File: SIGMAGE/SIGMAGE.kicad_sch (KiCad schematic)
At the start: 0 parts

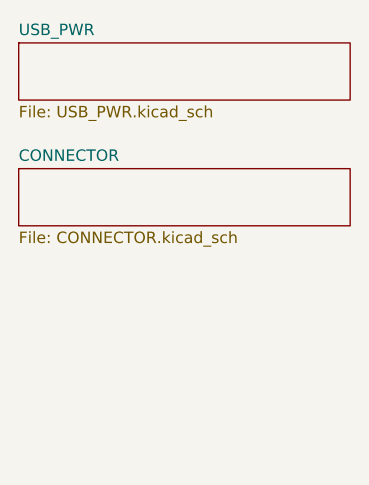
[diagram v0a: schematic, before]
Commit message: Added RJ45/PHY and MCU
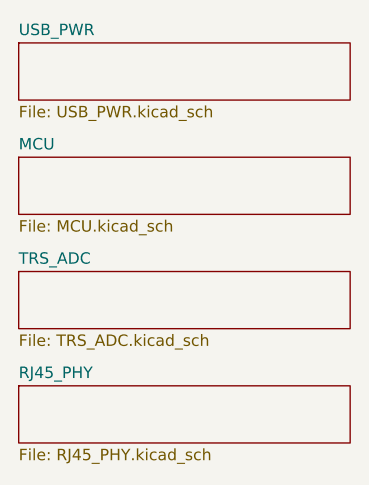
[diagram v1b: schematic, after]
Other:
- removed sheet CONNECTOR
- added sheet MCU (MCU.kicad_sch)
- added sheet RJ45_PHY (RJ45_PHY.kicad_sch)
- added sheet TRS_ADC (TRS_ADC.kicad_sch)
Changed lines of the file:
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@@
 	(paper "A4")
+	(sheet
+		(at 17.78 31.75)
+		(size 36.83 6.35)
+		(exclude_from_sim no)
+		(in_bom yes)
+		(on_board yes)
+		(dnp no)
+		(fields_autoplaced yes)
+		(stroke
+			(width 0.1524)
+			(type solid)
+		)
+		(fill
+			(color 0 0 0 0.0000)
+		)
+		(property "Sheetname" "MCU"
+			(at 17.78 31.0384 0)
+			(effects
+				(font
+					(size 1.27 1.27)
+				)
+				(justify left bottom)
+			)
+		)
+		(property "Sheetfile" "MCU.kicad_sch"
+			(at 17.78 38.6846 0)
+			(effects
+				(font
+					(size 1.27 1.27)
+				)
+				(justify left top)
+			)
+		)
+		(instances
+			(project "SIGMAGE"
+				(path "/6fbe3371-b6a3-4e28-aef4-4e5865f4674e"
+					(page "4")
+				)
+			)
+		)
+	)
 	(sheet
 		(at 17.78 19.05)
@@
 	)
 	(sheet
-		(at 17.78 33.02)
+		(at 17.78 44.45)
 		(size 36.83 6.35)
 		(exclude_from_sim no)
@@
 			(color 0 0 0 0.0000)
 		)
-		(property "Sheetname" "CONNECTOR"
-			(at 17.78 32.3084 0)
+		(property "Sheetname" "TRS_ADC"
+			(at 17.78 43.7384 0)
 			(effects
 				(font
@@
 			)
 		)
-		(property "Sheetfile" "CONNECTOR.kicad_sch"
-			(at 17.78 39.9546 0)
+		(property "Sheetfile" "TRS_ADC.kicad_sch"
+			(at 17.78 51.3846 0)
 			(effects
 				(font
@@
 			(project "SIGMAGE"
 				(path "/6fbe3371-b6a3-4e28-aef4-4e5865f4674e"
-					(page "3")
+					(page "5")
 				)
 			)
+		)
+	)
+	(sheet
+		(at 17.78 57.15)
+		(size 36.83 6.35)
+		(exclude_from_sim no)
+		(in_bom yes)
+		(on_board yes)
+		(dnp no)
+		(fields_autoplaced yes)
+		(stroke
+			(width 0.1524)
+			(type solid)
+		)
+		(fill
+			(color 0 0 0 0.0000)
+		)
+		(property "Sheetname" "RJ45_PHY"
+			(at 17.78 56.4384 0)
+			(effects
+				(font
+					(size 1.27 1.27)
+				)
+				(justify left bottom)
+			)
+		)
+		(property "Sheetfile" "RJ45_PHY.kicad_sch"
+			(at 17.78 64.0846 0)
+			(effects
+				(font
+					(size 1.27 1.27)
+				)
+				(justify left top)
+			)
+		)
+		(instances
+			(project "SIGMAGE"
+				(path "/6fbe3371-b6a3-4e28-aef4-4e5865f4674e"
+					(page "5")
+				)
+			)
